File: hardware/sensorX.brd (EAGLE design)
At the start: 106.7 x 13.7 mm, 37 parts

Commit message: shrunk board
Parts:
- removed 5V_IN, GND_IN: WIREPAD3,17/1,2, wirepad:3,17/1,2
- added 5V, GND: WIREPAD3,17/1,2, wirepad:3,17/1,2
- moved 1 6.03 mm to (39.4, 6.86)
- moved 3 6.03 mm to (28.8, 6.86)
- moved 5V_1 6.03 mm to (49.1, 3.05)
- moved 5V_2 6.03 mm to (57.2, 3.05)
- moved GND-1 6.03 mm to (49.1, 10.7)
- moved GND_2 6.03 mm to (57.2, 10.7)
- moved R1 6.03 mm to (38.5, 3.17)
- moved 4 6.03 mm to (23.4, 6.86)
- moved 5 6.03 mm to (18.1, 6.86)
- moved 6 6.03 mm to (12.8, 6.86)
- moved 7 6.03 mm to (7.43, 6.86)
- moved R3 6.03 mm to (27.8, 3.17)
- moved R4 6.03 mm to (22.5, 3.17)
- moved R5 6.03 mm to (17.1, 3.17)
- moved R7 6.03 mm to (6.48, 3.17)
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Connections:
- net +5V: now also 5V.1; no longer 5V_IN.1
- net GND: now also GND.1; no longer GND_IN.1
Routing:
- net +5V: track 102.5 -> 96.8 mm
- net GND: track 105.4 -> 100.2 mm
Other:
- board size 106.7 x 13.7 mm -> 99.8 x 13.7 mm

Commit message: fixed overlap
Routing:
- net SENSOR4: track 55.2 -> 56.4 mm
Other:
- board text added: "Rev C"
- board text removed: "Rev B"
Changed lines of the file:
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@@
 <?xml version="1.0" encoding="utf-8"?>
 <!DOCTYPE eagle SYSTEM "eagle.dtd">
-<eagle version="6.5.0">
+<eagle version="7.2.0">
 <drawing>
 <settings>
@@
 <text x="31.8902" y="11.811" size="1.27" layer="21" font="vector">SensorX</text>
 <text x="80.7852" y="0.254" size="0.8128" layer="21" font="vector">www.autosportlabs.net</text>
-<text x="95.5172" y="0.254" size="0.8128" layer="21" font="vector">Rev B</text>
+<text x="95.5172" y="0.254" size="0.8128" layer="21" font="vector">Rev C</text>
 <rectangle x1="23.4612" y1="11.4542" x2="30.5478" y2="11.4668" layer="21"/>
 <rectangle x1="23.4612" y1="11.4669" x2="30.5478" y2="11.4795" layer="21"/>
@@
 <pass name="Default">
 <param name="RoutingGrid" value="50mil"/>
+<param name="AutoGrid" value="1"/>
+<param name="Efforts" value="0"/>
+<param name="TopRouterVariant" value="1"/>
 <param name="tpViaShape" value="round"/>
 <param name="PrefDir.1" value="|"/>
@@
 <wire x1="48.451" y1="5.334" x2="50.102" y2="5.334" width="0.3048" layer="16"/>
 <wire x1="46.165" y1="3.048" x2="48.451" y2="5.334" width="0.3048" layer="16"/>
-<wire x1="27.242" y1="3.048" x2="46.165" y2="3.048" width="0.3048" layer="16"/>
-<wire x1="23.432" y1="6.858" x2="27.242" y2="3.048" width="0.3048" layer="16"/>
+<wire x1="25.146" y1="3.048" x2="46.165" y2="3.048" width="0.3048" layer="16"/>
 <contactref element="R4" pad="2"/>
 <wire x1="20.683446875" y1="4.97105" x2="22.570396875" y2="6.858" width="0.3048" layer="1"/>
 <wire x1="22.570396875" y1="6.858" x2="23.432" y2="6.858" width="0.3048" layer="1"/>
+<wire x1="25.146" y1="3.048" x2="23.432" y2="4.762" width="0.3048" layer="16"/>
+<wire x1="23.432" y1="4.762" x2="23.432" y2="6.858" width="0.3048" layer="16"/>
 </signal>
 <signal name="SENSOR5">

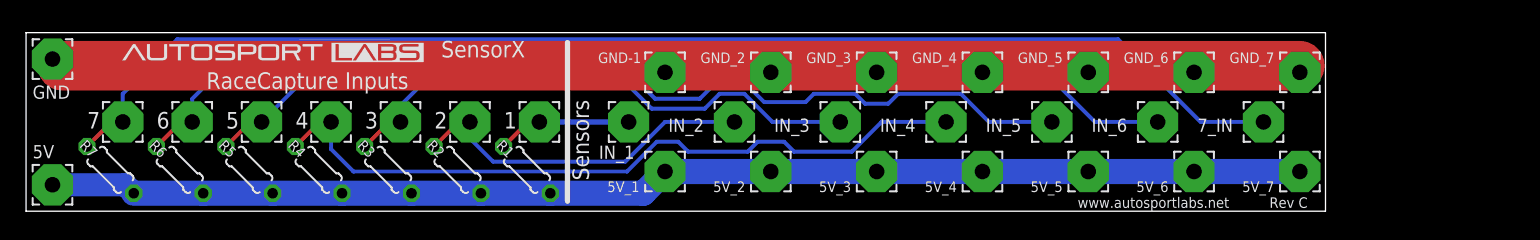
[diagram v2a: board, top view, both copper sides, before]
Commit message: add 8th sensor position
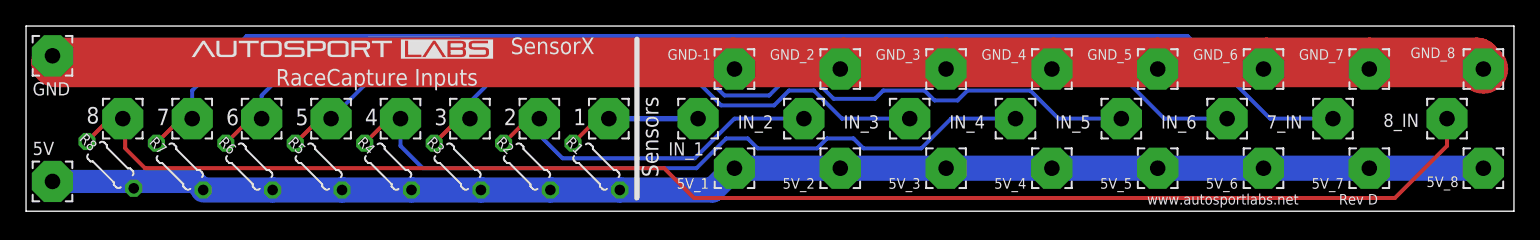
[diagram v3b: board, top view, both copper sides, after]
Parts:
- added 5V_8, 8, 8_IN, GND_8: WIREPAD3,17/1,2, wirepad:3,17/1,2
- added R8: 2.2K, rcl:0204/5
- moved 1 5.34 mm to (44.8, 7.11)
- moved 3 5.34 mm to (34.1, 7.11)
- moved 5V_1 5.34 mm to (54.4, 3.30)
- moved 5V_2 5.34 mm to (62.5, 3.30)
- moved 5V_3 5.34 mm to (70.7, 3.30)
- moved 5V_4 5.34 mm to (78.8, 3.30)
- moved 5V_5 5.34 mm to (86.9, 3.30)
- moved 5V_6 5.34 mm to (95.1, 3.30)
- moved 5V_7 5.34 mm to (103.2, 3.30)
- moved 7_IN 5.34 mm to (100.4, 7.11)
- moved GND-1 5.34 mm to (54.4, 10.9)
- moved GND_2 5.34 mm to (62.5, 10.9)
- moved GND_3 5.34 mm to (70.7, 10.9)
- moved GND_4 5.34 mm to (78.8, 10.9)
- moved GND_5 5.34 mm to (86.9, 10.9)
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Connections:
- new net SENSOR8: 8.1, 8_IN.1, R8.2
- net +5V: now also 5V_8.1, R8.1
- net GND: now also GND_8.1
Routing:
- net SENSOR8: track 0.00 -> 112.7 mm
- net GND: track 100.2 -> 124.9 mm
- net +5V: track 96.8 -> 111.6 mm
- net SENSOR3: track 40.0 -> 41.3 mm
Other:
- board size 99.8 x 13.7 mm -> 114.3 x 14.2 mm
- board text added: "Rev D"
- board text removed: "Rev C"
